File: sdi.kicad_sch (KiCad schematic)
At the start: 0 parts

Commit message: Added input and output termination
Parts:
- added C? (x2): C_1u_0402, antmicro-footprints:0402-cap, symbol antmicroCapacitors0402:C_1u_0402
- added C? (x2): C_4u7_0402, antmicro-footprints:0402-cap, symbol antmicroCapacitors0402:C_4u7_0402
- added C?: C_10n_0402, antmicro-footprints:0402-cap, symbol antmicroCapacitors0402:C_10n_0402
- added J? (x2): 031-70526-21, antmicro-footprints:BNC_Edge_Conn, symbol antmicroCoaxialConnectorsRF:031-70526-21
- added L? (x2): L_0402_6n2, antmicro-footprints:0402-cap, symbol antmicroFixedInductors:L_0402_6n2
- added R?: R_37R4_0402, antmicro-footprints:0402-res, symbol antmicroResistors0402:R_37R4_0402
- added R? (x6): R_75R_0402, antmicro-footprints:0402-res, symbol antmicroResistors0402:R_75R_0402
- added U? (x3): GS2971A, antmicro-footprints:BGA100_11x11mm, symbol antmicroInterfaceControllers:GS2971A
- added U?: GS2988, antmicro-footprints:QFN-16_EP_4x4_Pitch0.65mm, symbol antmicroInterfaceControllers:GS2988
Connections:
- new net: C?.1, R?.2
- new net: L?.1, R?.1, R?.2, U?.11 (~{SDO})
- new net: C?.1, L?.2, R?.2
- new net: C?.2, J?.1 (In)
- new net: C?.2, R?.1
- new net: J?.1 (In), L?.1, R?.1
- new net: C?.1, L?.2, R?.2, R?.2
- new net: C?.1, R?.1, U?.12 (SDO)
- new net +3V3: C?.2, R?.1, R?.2, U?.9 (VCC)
- new net GND: C?.1, J?.2 (Ext), J?.2 (Ext), R?.1, R?.1, R?.2
- new net SDI: C?.2
- new net SDI_D0: U?.K8 (DOUT0)
- new net SDI_D1: U?.J8 (DOUT01)
- new net SDI_D10: U?.E9 (DOUT10)
- new net SDI_D11: U?.E10 (DOUT11)
- new net SDI_D12: U?.C8 (DOUT12)
- new net SDI_D13: U?.C10 (DOUT13)
- new net SDI_D14: U?.C9 (DOUT14)
- new net SDI_D15: U?.B10 (DOUT15)
- new net SDI_D16: U?.B9 (DOUT16)
- new net SDI_D17: U?.A10 (DOUT17)
- new net SDI_D18: U?.A9 (DOUT18)
- new net SDI_D19: U?.B8 (DOUT19)
- new net SDI_D2: U?.K9 (DOUT02)
- new net SDI_D3: U?.K10 (DOUT03)
- new net SDI_D4: U?.J9 (DOUT04)
- new net SDI_D5: U?.J10 (DOUT05)
- new net SDI_D6: U?.H9 (DOUT06)
- new net SDI_D7: U?.H10 (DOUT07)
- new net SDI_D8: U?.F9 (DOUT08)
- new net SDI_D9: U?.F10 (DOUT09)
- new net ~{SDI}: C?.2

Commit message: Connected Semtech to the power supply, cable driver and the FPGA
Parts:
- added C73, C74, C75, C76, C77, C78, C79, C80, C81, C82, C83, C84, C85: C_100n_0603, antmicro-footprints:0603-cap, symbol antmicroCapacitors0603:C_100n_0603
- added C89, C90: C_33p_0603, antmicro-footprints:0603-cap, symbol antmicroCapacitors0603:C_33p_0603
- added C91, C93: C_470n_0603, antmicro-footprints:0603-cap, symbol antmicroCapacitors0603:C_470n_0603
- added C92: C_47n_0603, antmicro-footprints:0603-cap, symbol antmicroCapacitors0603:C_47n_0603
- added C94: ~, symbol antmicroCapacitors0402:C_1u_0402
- added C95: C_33u_0603, antmicro-footprints:0603-cap, symbol antmicroCapacitorspol:C_33u_0603
- added R49, R50: R_100k_0603, antmicro-footprints:0603-res, symbol antmicroResistors0603:R_100k_0603
- added R51: R_105R_0402, antmicro-footprints:0402-res, symbol antmicroResistors0402:R_105R_0402
- added R?: R_750R_0603, antmicro-footprints:0603-res, symbol antmicroResistors0603:R_750R_0603
- added R?: R_0R_0603, antmicro-footprints:0603-res, symbol antmicroResistors0603:R_0R_0603
- added TP12, TP?: TP, antmicro-footprints:TP-R-1.5, symbol antmicroTestPoints:TP
- added Y1: ABM7_27.000MH_D2Y_T, antmicro-footprints:ABM7_OSC, symbol antmicroOscillators:ABM7_27.000MH_D2Y_T
- C71, C72: renamed from C?; value C_1u_0402 -> (none); footprint antmicro-footprints:0402-cap -> (none)
- C86: renamed from C?; value C_10n_0402 -> (none); footprint antmicro-footprints:0402-cap -> (none)
- C87, C88: renamed from C?; value C_4u7_0402 -> (none); footprint antmicro-footprints:0402-cap -> (none)
- J4, J5: renamed from J?; value 031-70526-21 -> (none); footprint antmicro-footprints:BNC_Edge_Conn -> (none)
- L4, L5: renamed from L?; value L_0402_6n2 -> (none); footprint antmicro-footprints:0402-cap -> (none)
- R42, R43, R45, R46, R47, R48: renamed from R?; value R_75R_0402 -> (none); footprint antmicro-footprints:0402-res -> (none)
- R44: renamed from R?; value R_37R4_0402 -> (none); footprint antmicro-footprints:0402-res -> (none)
- U11: renamed from U?; value GS2988 -> (none); footprint antmicro-footprints:QFN-16_EP_4x4_Pitch0.65mm -> (none)
- gave numbers to parts that had none: 1
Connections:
- net SDI is gone; now on net SDI_P: C71.2
- net ~{SDI} is gone; now on net SDI_N: C72.2
- net +3V3: now also U10.A7 (IO_VDD), U10.B1 (A_VDD), U10.D10 (IO_VDD), U10.E1 (EQ_VDD), U10.G10 (IO_VDD), U10.H1 (BUFF_VDD), U10.K7 (IO_VDD), C73.1, C75.1, C77.1, C79.1, C81.1, C83.1, C85.1, R50.2, R?.2, R?.2
- net GND: now also U10.B4 (VCO_GND), U10.B7 (IO_GND), U10.C2 (A_GND), U10.D2 (A_GND), U10.D3 (A_GND), U10.D4 (PLL_GND), U10.D5 (CORE_GND), U10.D9 (IO_GND), U10.E2 (EQ_GND), U10.E3 (A_GND), U10.E4 (PLL_GND), U10.E5 (CORE_GND), U10.F3 (A_GND), U10.F4 (PLL_GND), U10.F5 (CORE_GND), U10.G2 (A_GND), U10.G4 (CORE_GND), U10.G5 (CORE_GND), U10.G9 (IO_GND), U10.H2 (BUFF_GND), U10.J7 (IO_GND), U11.10 (SD/~{HD}), U11.17 (C_PAD), U11.3 (VEE), C73.2, C74.2, C75.2, C76.2, C77.2, C78.2, C79.2, C80.2, C81.2, C82.2, C83.2, C84.2, C85.2, C89.1, C90.1, C91.2, C92.2, C94.2, C95.2, R49.1
- net at U10.A4 (VCO_VDD): now also C95.1, R51.2
- net +1V2: now reaches U10.B2 (PLL_VDD)
- net +1V2: now also U10.C3 (PLL_VDD), U10.C4 (PLL_VDD), U10.D6 (CORE_VDD), U10.E6 (CORE_VDD), U10.F6 (CORE_VDD), U10.G6 (CORE_VDD), C74.1, C76.1, C78.1, C80.1, C82.1, C84.1, R51.1
- net SDI_STAT0: now reaches U10.A5 (STAT0)
- net SDI_STAT1: now reaches U10.A6 (STAT1)
- net SDI_PCLK: now reaches U10.A8 (PCLK)
- net SDI_STAT2: now reaches U10.B5 (STAT2)
- net SDI_STAT3: now reaches U10.B6 (STAT3)
- net SDI_STAT4: now reaches U10.C5 (STAT4)
- net SDI_STAT5: now reaches U10.C6 (STAT5)
- net AUDIO_WCLK: now reaches U10.H4 (WCLK)
- net SDO_P: now reaches U10.J1 (SDO)
- net SDO_P: now also U11.1 (DDI)
- net AUDIO_OUT_CH1_2: now reaches U10.J3 (AOUT_1/2)
- net AUDIO_ACLK: now reaches U10.J4 (ACLK)
- net AUDIO_OUT_CH5_6: now reaches U10.J5 (AOUT_5/6)
- net SDO_N: now reaches U10.K1 (~{SDO})
- net SDO_N: now also U11.2 (~{DDI})
- net AUDIO_OUT_CH3_4: now reaches U10.K3 (AOUT_3/4)
- net AUDIO_MCLK: now reaches U10.K4 (AMCLK)
- net AUDIO_OUT_CH7_8: now reaches U10.K5 (AOUT_7/8)
- net at R45.2, R47.1, U11.11 (~{SDO}): now also L5.2; no longer L5.1
- net at C88.1, R47.2: now also L5.1; no longer L5.2
- net at J4.1 (In), R42.1: now also L4.2; no longer L4.1
- net at C71.1, R42.2, R43.2: now also L4.1; no longer L4.2
- net at U10.A1 (VBG): now also C94.1
- net at U10.A2 (LF): now also C92.1
- net at U10.A3 (LB_CONT): now also R49.2, R50.1
- net SDI_P: now reaches U10.C1 (SDI)
- net RESET_TRST: now reaches U10.C7 (RESET_TRST)
- net SDI_N: now reaches U10.D1 (~{SDI})
- net SW_EN: now reaches U10.D7 (SW_EN)
- net JTAG/~{HOST}: now reaches U10.D8 (JTAG/~{HOST})
- net SDOUT_TDO: now reaches U10.E7 (SDOUT_TDO)
- net SDIN_TDI: now reaches U10.E8 (SDIN_TDI)
- net at U10.F1 (AGCP): now also C93.2
- net ~{CS_TMS}: now reaches U10.F7 (~{CS}_TMS)
- net SCLK_TCK: now reaches U10.F8 (SCLK_TCK)
- net at U10.G1 (AGCN): now also C91.1, C93.1
- net ~{RC_BYP}: now reaches U10.G3 (~{RC_BYP})
- net ~{SMPTE_BYPASS}: now reaches U10.G7 (~{SMPTE_BYPASS})
- net DVB_ASI: now reaches U10.G8 (DVB_ASI)
- net AUDIO_EN/~{DIS}: now reaches U10.H3 (AUDIO_EN/~{DIS})
- net TIM_861: now reaches U10.H5 (TIM_861)
- net at U10.H6 (XTAL_OUT): now also TP12.1
- net 20bit/~{10bit}: now reaches U10.H7 (20bit/~{10bit})
- net IOPROC_EN/~{DIS}: now reaches U10.H8 (IOPROC_EN/~{DIS})
- net SDO_EN/DIS: now reaches U10.J2 (SDO_EN/DIS)
- net XTAL2: now reaches U10.J6 (XTAL2)
- net XTAL2: now also C90.2, Y1.1
- net STANDBY: now reaches U10.K2 (STANDBY)
- net XTAL1: now reaches U10.K6 (XTAL1)
- net XTAL1: now also C89.2, Y1.2
- net at U11.14 (~{OSP}): now also TP?.1
- net at U11.16 (~{EQ_EN}): now also R?.1
- net at U11.4 (RSET): now also R?.1
- net ~{SDO_DISABLE}: now reaches U11.6 (~{DISABLE})
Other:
- note added: "Cable driver"
- note added: "SDI Receiver"
- moved on the sheet: C71, C72, C86, C87, C88, J4, J5, L4, L5, R42, R43, R44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

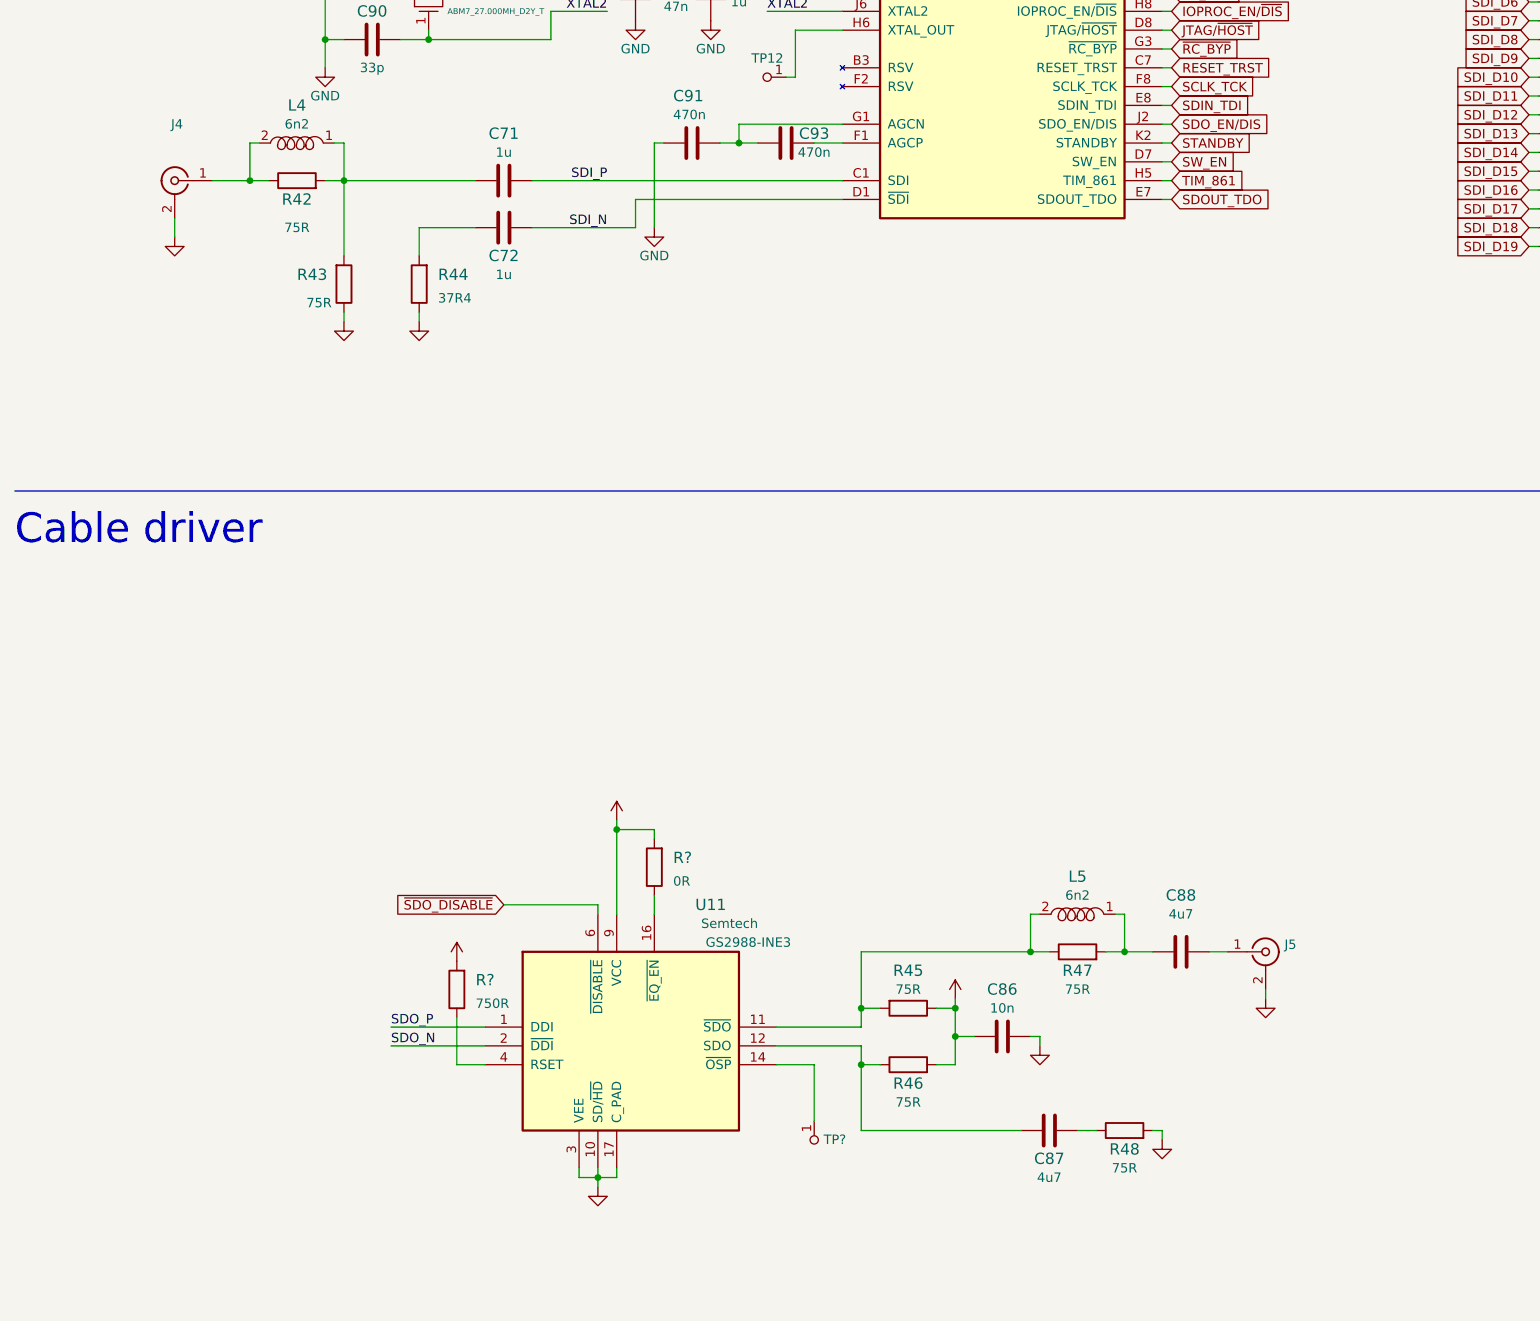
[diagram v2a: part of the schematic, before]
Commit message: Added FPGA configuration circuitry
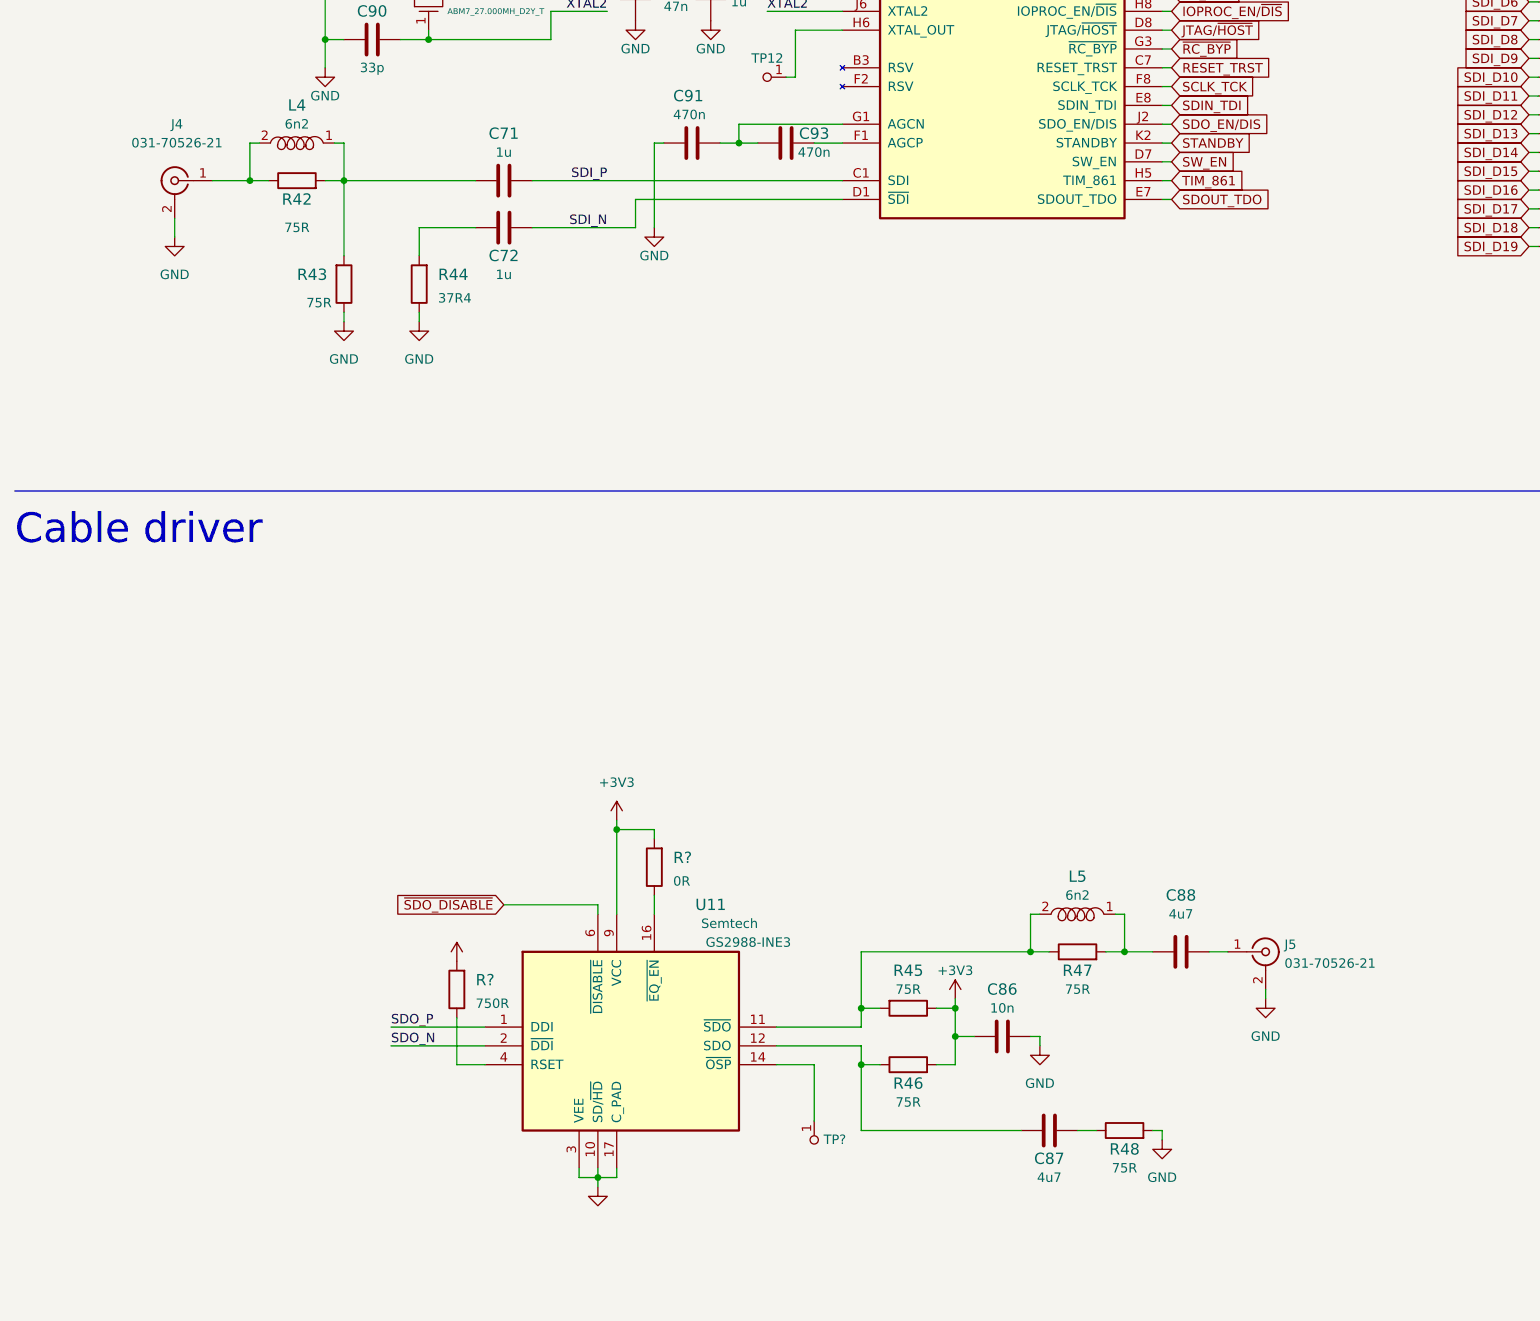
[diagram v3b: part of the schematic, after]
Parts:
- C71, C72: value (none) -> C_1u_0402; footprint (none) -> antmicro-footprints:0402-cap
- C86: value (none) -> C_10n_0402; footprint (none) -> antmicro-footprints:0402-cap
- C87, C88: value (none) -> C_4u7_0402; footprint (none) -> antmicro-footprints:0402-cap
- J4, J5: value (none) -> 031-70526-21; footprint (none) -> antmicro-footprints:BNC_Edge_Conn
- L4, L5: value (none) -> L_0402_6n2; footprint (none) -> antmicro-footprints:0402-cap
- R42, R43, R45, R46, R47, R48: value (none) -> R_75R_0402; footprint (none) -> antmicro-footprints:0402-res
- R44: value (none) -> R_37R4_0402; footprint (none) -> antmicro-footprints:0402-res
- U11: value (none) -> GS2988; footprint (none) -> antmicro-footprints:QFN-16_EP_4x4_Pitch0.65mm

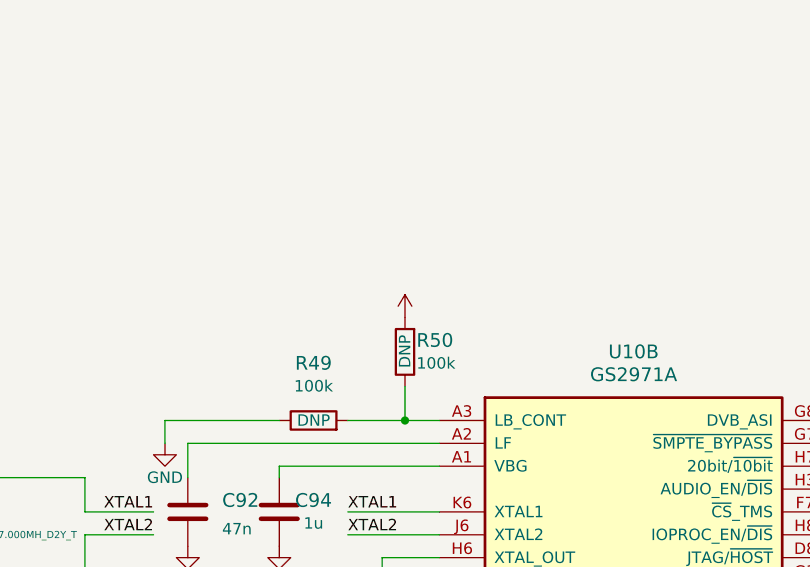
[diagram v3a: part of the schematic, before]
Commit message: Replaced RPi camera connector with 50pin one, modified PSU with ability of being supplied via FFC
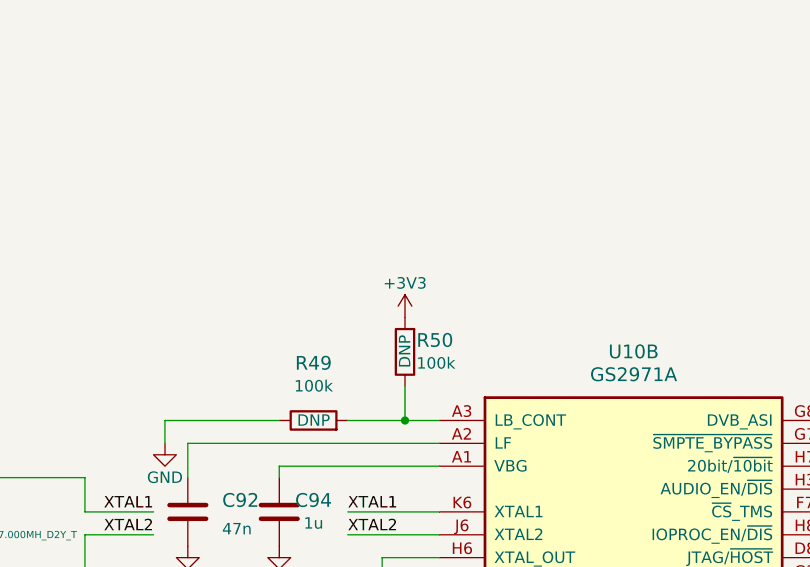
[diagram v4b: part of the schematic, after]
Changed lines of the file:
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@@
-    (pin "1")
-  )
-  (symbol (lib_id "power:+3V3") (at 120.65 57.15 0) (unit 1)
-    (in_bom yes) (on_board yes) (fields_autoplaced)
-    (property "Reference" "#PWR0252" (id 0) (at 120.65 60.96 0)
-      (effects (font (size 1.27 1.27)) hide)
-    )
-    (property "Value" "~" (id 1) (at 120.65 52.07 0))
-    (property "Footprint" "" (id 2) (at 120.65 57.15 0)
-      (effects (font (size 1.27 1.27)) hide)
-    )
-    (property "Datasheet" "" (id 3) (at 120.65 57.15 0)
-      (effects (font (size 1.27 1.27)) hide)
-    )
     (pin "1")
   )
@@
     (pin "2")
   )
+  (symbol (lib_id "power:+3V3") (at 120.65 57.15 0) (unit 1)
+    (in_bom yes) (on_board yes)
+    (property "Reference" "#PWR?" (id 0) (at 120.65 60.96 0)
+      (effects (font (size 1.27 1.27)) hide)
+    )
+    (property "Value" "+3V3" (id 1) (at 120.65 53.34 0))
+    (property "Footprint" "" (id 2) (at 120.65 57.15 0)
+      (effects (font (size 1.27 1.27)) hide)
+    )
+    (property "Datasheet" "" (id 3) (at 120.65 57.15 0)
+      (effects (font (size 1.27 1.27)) hide)
+    )
+    (pin "1")
+  )
   (symbol (lib_id "power:GND") (at 167.64 233.68 0) (unit 1)

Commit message: Made PCB mockup
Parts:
- removed C94: ~, symbol antmicroCapacitors0402:C_1u_0402
- added C49: C_1u_0402, antmicro-footprints:0402-cap, symbol antmicroCapacitors0402:C_1u_0402
- gave numbers to parts that had none: 3
- renumbered C89 to C43, C90 to C44, C71 to C45, C72 to C46, C92 to C47, C91 to C48, C93 to C50, C86 to C51, C87 to C52, C88 to C53, C73 to C54, C74 to C55, C75 to C56, C76 to C57, C77 to C58, C78 to C59, C79 to C60, C80 to C61, C81 to C62, C95 to C63, C82 to C64, C83 to C65, C84 to C66, C85 to C67, J4 to J2, J5 to J3, R42 to R55, R43 to R56, R44 to R57, R49 to R60, R50 to R61, R45 to R62, R46 to R63, R47 to R64, R48 to R65, R51 to R66, TP12 to TP14, U11 to U9
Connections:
- net GND: now also C49.1
- net at U10.A1 (VBG): now also C49.2
